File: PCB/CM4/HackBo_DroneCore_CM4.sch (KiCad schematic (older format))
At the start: 0 parts

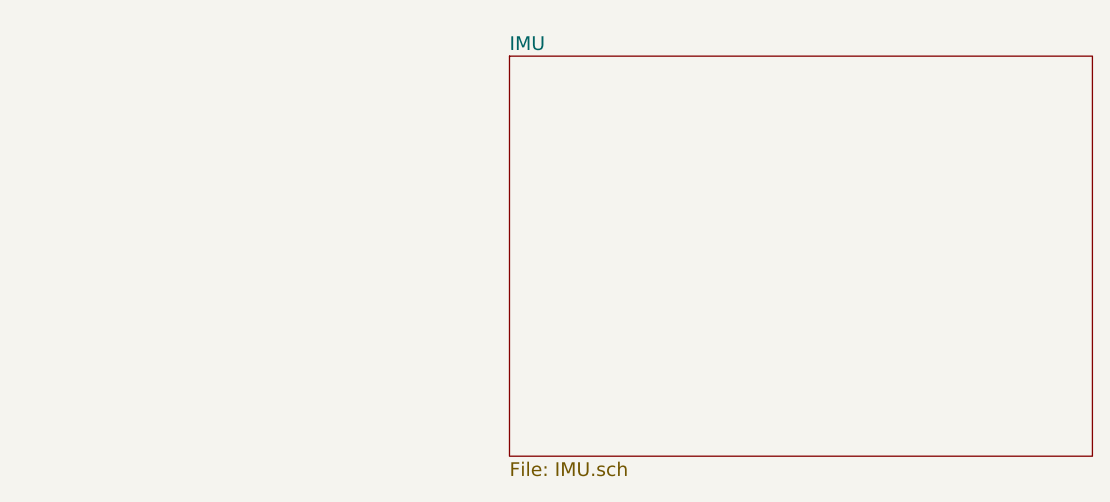
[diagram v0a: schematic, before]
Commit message: Cortex M4 hasbeen placed, decoupling Caps too
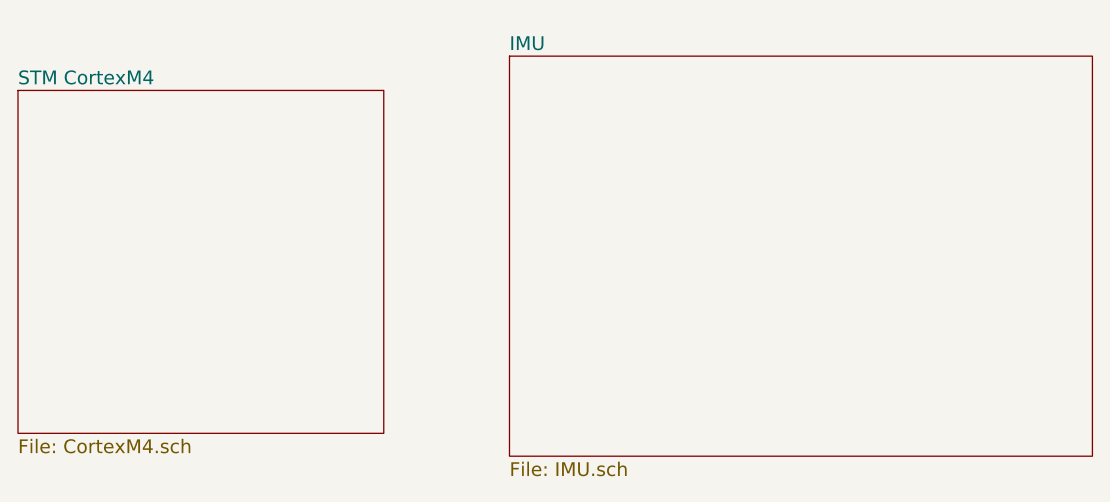
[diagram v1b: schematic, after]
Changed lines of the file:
@@
-EESchema Schematic File Version 2  date Fri 02 Nov 2012 01:03:51 PM COT
+EESchema Schematic File Version 2  date Sat 03 Nov 2012 06:00:55 PM COT
 LIBS:power
 LIBS:device
@@
 LIBS:mpu6050
 LIBS:stm32f100vxx
-EELAYER 43  0
+LIBS:HackBo_DroneCore_CM4-cache
+EELAYER 25  0
 EELAYER END
 $Descr A4 11693 8268
 encoding utf-8
-Sheet 1 2
+Sheet 1 3
 Title ""
-Date "2 nov 2012"
+Date "3 nov 2012"
 Rev ""
 Comp ""
@@
 F1 "IMU.sch" 60
 $EndSheet
+$Sheet
+S 3150 2550 1600 1500
+U 50940D21
+F0 "STM CortexM4" 60
+F1 "CortexM4.sch" 60
+$EndSheet
 $EndSCHEMATC

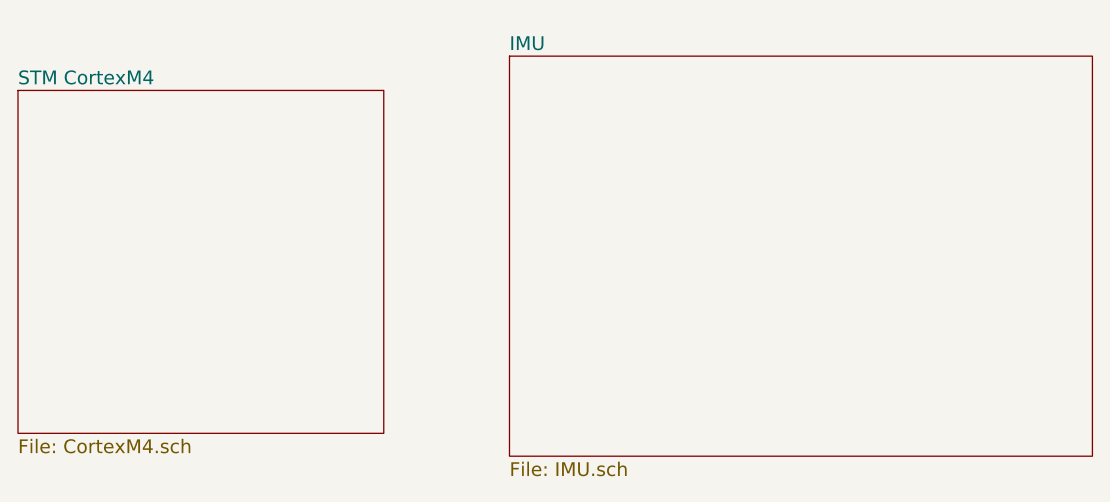
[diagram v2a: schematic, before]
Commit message: IMU caps decoupling
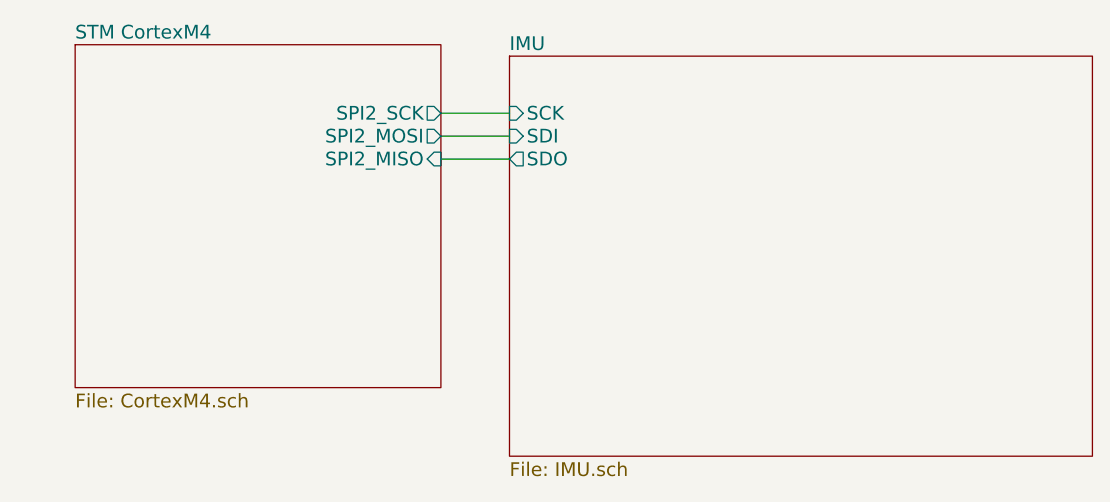
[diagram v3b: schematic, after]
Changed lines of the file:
@@
-EESchema Schematic File Version 2  date Sat 03 Nov 2012 06:26:30 PM COT
+EESchema Schematic File Version 2  date Sat 03 Nov 2012 06:56:08 PM COT
 LIBS:power
 LIBS:device
@@
 F0 "IMU" 60
 F1 "IMU.sch" 60
+F2 "SDI" I L 5300 2750 60
+F3 "SCK" I L 5300 2650 60
+F4 "SDO" O L 5300 2850 60
 $EndSheet
 $Sheet
-S 3150 2550 1600 1500
+S 3400 2350 1600 1500
 U 50940D21
 F0 "STM CortexM4" 60
 F1 "CortexM4.sch" 60
+F2 "SPI2_MOSI" O R 5000 2750 60
+F3 "SPI2_MISO" I R 5000 2850 60
+F4 "SPI2_SCK" O R 5000 2650 60
 $EndSheet
+Wire Wire Line
+	5000 2650 5300 2650
+Wire Wire Line
+	5000 2750 5300 2750
+Wire Wire Line
+	5000 2850 5300 2850
 $EndSCHEMATC
